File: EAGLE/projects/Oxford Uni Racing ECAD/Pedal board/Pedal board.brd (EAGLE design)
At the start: 165.1 x 216.8 mm, 40 parts, among them IC1 AD711N, J1 ASS + BOTS, J2 THR_1_2, J3 PWR_CAN, J6 BR_POS_PRESS_STWH, J7 T821108A1S100CEU, K2 EC2-12TNU, T1 BT169, X2 D-SUB9-H2M09ST

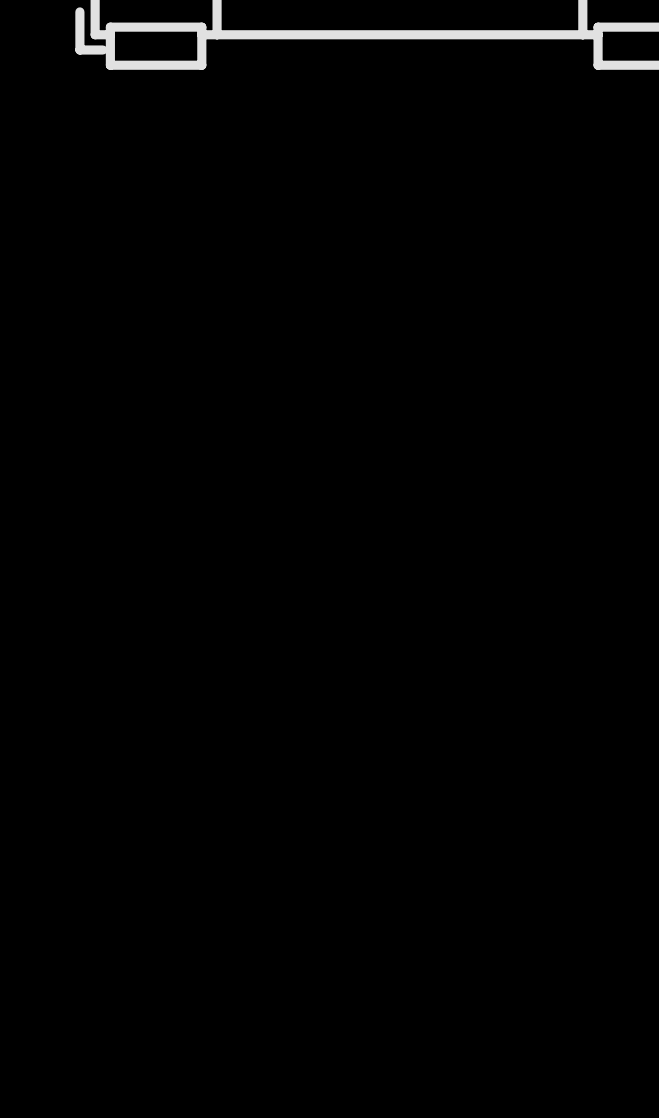
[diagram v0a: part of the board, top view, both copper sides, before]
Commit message: added 1M pullup resistors to analog sensors
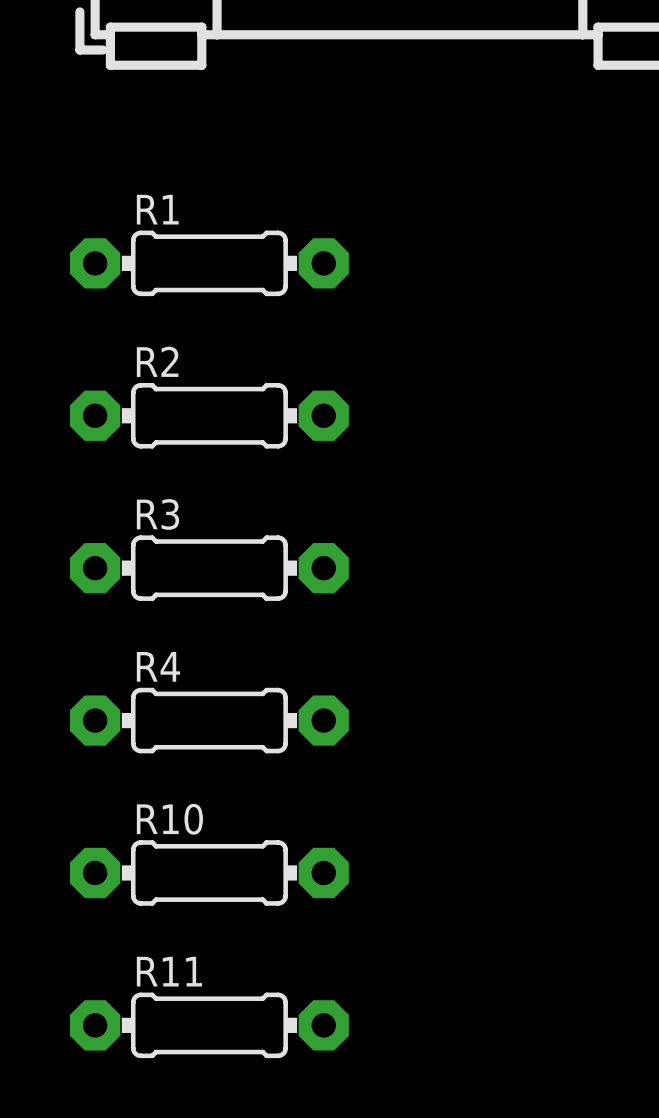
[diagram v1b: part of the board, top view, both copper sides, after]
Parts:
- added R1, R10, R11, R2, R3, R4: 1M, adafruit:0204/7
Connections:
- net 5V: now also R1.2, R10.1, R11.1, R2.1, R3.2, R4.2
- net BR_POSS: now also R10.2
- net BR_POSS2: now also R4.1
- net N$27: now also R11.2
- net ST_WH_POSS: now also R3.1
- net THR1: now also R1.1
- net THR2: now also R2.2
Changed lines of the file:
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@@
 <attribute name="VALUE" x="-74.422" y="-253.492" size="2.54" layer="27"/>
+</element>
+<element name="R1" library="adafruit" library_urn="urn:adsk.eagle:library:420" package="0204/7" package3d_urn="urn:adsk.eagle:package:6240596/1" value="1M" x="-74.93" y="-257.81" smashed="yes">
+<attribute name="NAME" x="-77.47" y="-256.5146" size="0.9906" layer="25" ratio="12"/>
+<attribute name="VALUE" x="-76.5556" y="-258.2926" size="0.9906" layer="27" ratio="12"/>
+</element>
+<element name="R2" library="adafruit" library_urn="urn:adsk.eagle:library:420" package="0204/7" package3d_urn="urn:adsk.eagle:package:6240596/1" value="1M" x="-74.93" y="-262.89" smashed="yes">
+<attribute name="NAME" x="-77.47" y="-261.5946" size="0.9906" layer="25" ratio="12"/>
+<attribute name="VALUE" x="-76.5556" y="-263.3726" size="0.9906" layer="27" ratio="12"/>
+</element>
+<element name="R3" library="adafruit" library_urn="urn:adsk.eagle:library:420" package="0204/7" package3d_urn="urn:adsk.eagle:package:6240596/1" value="1M" x="-74.93" y="-267.97" smashed="yes">
+<attribute name="NAME" x="-77.47" y="-266.6746" size="0.9906" layer="25" ratio="12"/>
+<attribute name="VALUE" x="-76.5556" y="-268.4526" size="0.9906" layer="27" ratio="12"/>
+</element>
+<element name="R4" library="adafruit" library_urn="urn:adsk.eagle:library:420" package="0204/7" package3d_urn="urn:adsk.eagle:package:6240596/1" value="1M" x="-74.93" y="-273.05" smashed="yes">
+<attribute name="NAME" x="-77.47" y="-271.7546" size="0.9906" layer="25" ratio="12"/>
+<attribute name="VALUE" x="-76.5556" y="-273.5326" size="0.9906" layer="27" ratio="12"/>
+</element>
+<element name="R10" library="adafruit" library_urn="urn:adsk.eagle:library:420" package="0204/7" package3d_urn="urn:adsk.eagle:package:6240596/1" value="1M" x="-74.93" y="-278.13" smashed="yes">
+<attribute name="NAME" x="-77.47" y="-276.8346" size="0.9906" layer="25" ratio="12"/>
+<attribute name="VALUE" x="-76.5556" y="-278.6126" size="0.9906" layer="27" ratio="12"/>
+</element>
+<element name="R11" library="adafruit" library_urn="urn:adsk.eagle:library:420" package="0204/7" package3d_urn="urn:adsk.eagle:package:6240596/1" value="1M" x="-74.93" y="-283.21" smashed="yes">
+<attribute name="NAME" x="-77.47" y="-281.9146" size="0.9906" layer="25" ratio="12"/>
+<attribute name="VALUE" x="-76.5556" y="-283.6926" size="0.9906" layer="27" ratio="12"/>
 </element>
 </elements>
@@
 <contactref element="U$1" pad="J802-4"/>
 <contactref element="R21" pad="E"/>
+<contactref element="R10" pad="1"/>
+<contactref element="R4" pad="2"/>
+<contactref element="R11" pad="1"/>
+<contactref element="R3" pad="2"/>
+<contactref element="R2" pad="1"/>
+<contactref element="R1" pad="2"/>
+<wire x1="-71.12" y1="-257.81" x2="-78.74" y2="-171.45" width="0" layer="19" extent="1-1"/>
+<wire x1="-78.74" y1="-262.89" x2="-71.12" y2="-257.81" width="0" layer="19" extent="1-1"/>
+<wire x1="-71.12" y1="-267.97" x2="-78.74" y2="-262.89" width="0" layer="19" extent="1-1"/>
+<wire x1="-71.12" y1="-273.05" x2="-71.12" y2="-267.97" width="0" layer="19" extent="1-1"/>
+<wire x1="-78.74" y1="-278.13" x2="-71.12" y2="-273.05" width="0" layer="19" extent="1-1"/>
+<wire x1="-78.74" y1="-283.21" x2="-78.74" y2="-278.13" width="0" layer="19" extent="1-1"/>
 <wire x1="5.715" y1="-204.47" x2="-78.74" y2="-171.45" width="0" layer="19" extent="1-1"/>
 <wire x1="8.89" y1="-118.11" x2="5.715" y2="-204.47" width="0" layer="19" extent="1-1"/>
@@
 <contactref element="J2" pad="5"/>
 <contactref element="U$1" pad="J803-0"/>
+<contactref element="R1" pad="1"/>
 <wire x1="-78.74" y1="-184.15" x2="152.4" y2="34.29" width="0" layer="19" extent="1-1"/>
+<wire x1="-78.74" y1="-257.81" x2="-78.74" y2="-184.15" width="0" layer="19" extent="1-1"/>
 </signal>
 <signal name="THR2">
 <contactref element="J2" pad="6"/>
 <contactref element="U$1" pad="J803-1"/>
+<contactref element="R2" pad="2"/>
 <wire x1="-78.74" y1="-186.69" x2="152.4" y2="36.83" width="0" layer="19" extent="1-1"/>
+<wire x1="-71.12" y1="-262.89" x2="-78.74" y2="-186.69" width="0" layer="19" extent="1-1"/>
 </signal>
 <signal name="3.3V">
@@
 <contactref element="J6" pad="5"/>
 <contactref element="U$1" pad="J803-3"/>
+<contactref element="R10" pad="2"/>
 <wire x1="-78.74" y1="-191.77" x2="13.97" y2="-120.65" width="0" layer="19" extent="1-1"/>
+<wire x1="-71.12" y1="-278.13" x2="-78.74" y2="-191.77" width="0" layer="19" extent="1-1"/>
 </signal>
 <signal name="BRAKE_LIGHTS_OUT">
@@
 <contactref element="J6" pad="6"/>
 <contactref element="IC1" pad="3"/>
+<contactref element="R11" pad="2"/>
 <wire x1="13.97" y1="-118.11" x2="7.62" y2="-171.45" width="0" layer="19" extent="1-1"/>
+<wire x1="-71.12" y1="-283.21" x2="7.62" y2="-171.45" width="0" layer="19" extent="1-1"/>
 </signal>
 <signal name="BR_PRESS">
@@
 <contactref element="J6" pad="7"/>
 <contactref element="U$1" pad="J803-4"/>
+<contactref element="R4" pad="1"/>
 <wire x1="-78.74" y1="-194.31" x2="16.51" y2="-120.65" width="0" layer="19" extent="1-1"/>
+<wire x1="-78.74" y1="-273.05" x2="-78.74" y2="-194.31" width="0" layer="19" extent="1-1"/>
 </signal>
 <signal name="ST_WH_POSS">
 <contactref element="J6" pad="8"/>
 <contactref element="U$1" pad="J803-5"/>
+<contactref element="R3" pad="1"/>
 <wire x1="-78.74" y1="-196.85" x2="16.51" y2="-118.11" width="0" layer="19" extent="1-1"/>
+<wire x1="-78.74" y1="-267.97" x2="-78.74" y2="-196.85" width="0" layer="19" extent="1-1"/>
 </signal>
 <signal name="12V_BATTERY">

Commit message: fixed overlapping digital pins
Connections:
- net BR_POSS: now also U$1.J803-2; no longer U$1.J803-3
- net BR_POSS2: now also U$1.J803-3; no longer U$1.J803-4
- net BR_PRESS: now also U$1.J803-4; no longer U$1.J803-2
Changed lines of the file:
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@@
 <signal name="BR_POSS">
 <contactref element="J6" pad="5"/>
-<contactref element="U$1" pad="J803-3"/>
 <contactref element="R10" pad="2"/>
-<wire x1="-78.74" y1="-191.77" x2="13.97" y2="-120.65" width="0" layer="19" extent="1-1"/>
-<wire x1="-71.12" y1="-278.13" x2="-78.74" y2="-191.77" width="0" layer="19" extent="1-1"/>
+<contactref element="U$1" pad="J803-2"/>
+<wire x1="-78.74" y1="-189.23" x2="13.97" y2="-120.65" width="0" layer="19" extent="1-1"/>
+<wire x1="-71.12" y1="-278.13" x2="-78.74" y2="-189.23" width="0" layer="19" extent="1-1"/>
 </signal>
 <signal name="BRAKE_LIGHTS_OUT">
@@
 <contactref element="COMPARATOR" pad="5"/>
 <wire x1="8.190228125" y1="-68.94195" x2="11.504928125" y2="-68.94195" width="0.8128" layer="16"/>
-<contactref element="U$1" pad="J803-2"/>
+<contactref element="U$1" pad="J803-4"/>
 <wire x1="7.62" y1="-181.61" x2="0" y2="-176.53" width="0" layer="19" extent="1-1"/>
-<wire x1="-78.74" y1="-189.23" x2="0" y2="-176.53" width="0" layer="19" extent="1-1"/>
+<wire x1="-78.74" y1="-194.31" x2="0" y2="-176.53" width="0" layer="19" extent="1-1"/>
 <wire x1="8.190228125" y1="-68.94195" x2="0" y2="-176.53" width="0" layer="19" extent="16-16"/>
 </signal>
@@
 <signal name="BR_POSS2">
 <contactref element="J6" pad="7"/>
-<contactref element="U$1" pad="J803-4"/>
 <contactref element="R4" pad="1"/>
-<wire x1="-78.74" y1="-194.31" x2="16.51" y2="-120.65" width="0" layer="19" extent="1-1"/>
-<wire x1="-78.74" y1="-273.05" x2="-78.74" y2="-194.31" width="0" layer="19" extent="1-1"/>
+<contactref element="U$1" pad="J803-3"/>
+<wire x1="-78.74" y1="-191.77" x2="16.51" y2="-120.65" width="0" layer="19" extent="1-1"/>
+<wire x1="-78.74" y1="-273.05" x2="-78.74" y2="-191.77" width="0" layer="19" extent="1-1"/>
 </signal>
 <signal name="ST_WH_POSS">

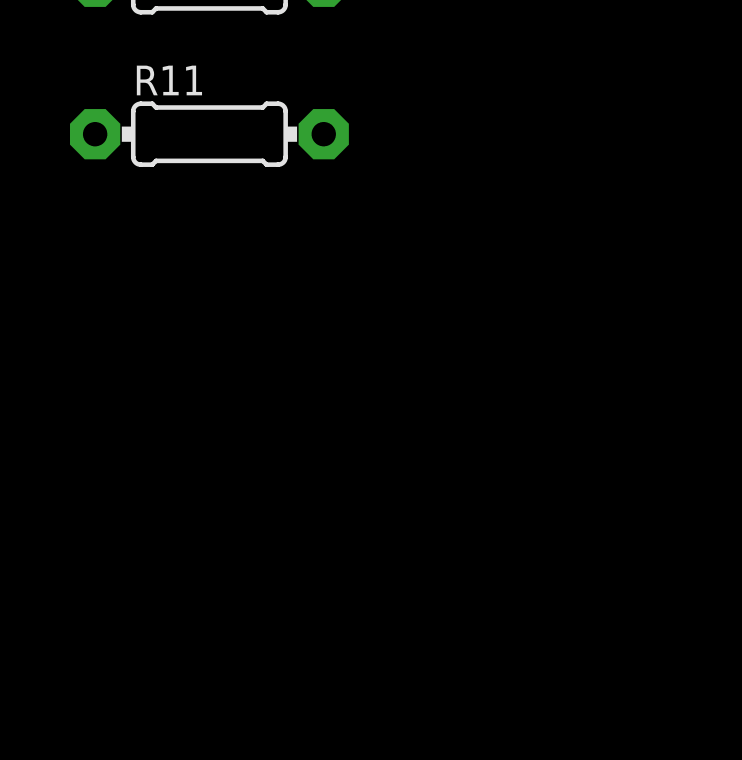
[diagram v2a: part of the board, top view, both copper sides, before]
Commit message: added indicator LEDs to boards
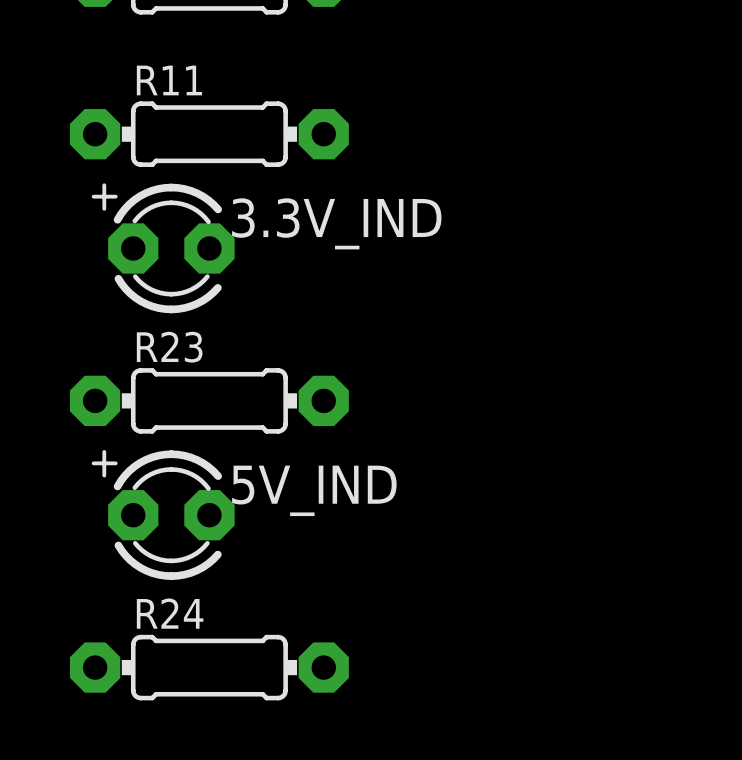
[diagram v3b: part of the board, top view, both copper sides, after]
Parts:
- added 3.3V_IND, 5V_IND: (no value), adafruit:LED3MM
- added R23, R24: (no value), adafruit:0204/7
- BRAKE_LIGHTS: value 2A -> 1A
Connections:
- new net N$12: 3.3V_IND.K, R23.2
- new net N$4: 5V_IND.K, R24.2
- net 3.3V: now also 3.3V_IND.A
- net 5V: now also 5V_IND.A
- net GND: now also R23.1, R24.1
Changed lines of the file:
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@@
 <attribute name="VALUE" x="-74.422" y="-238.252" size="2.54" layer="27"/>
 </element>
-<element name="BRAKE_LIGHTS" library="fuse" library_urn="urn:adsk.eagle:library:233" package="FUSE_HOLDER_5X20MM" package3d_urn="urn:adsk.eagle:package:14079/1" value="2A" x="-76.2" y="-247.65" smashed="yes">
+<element name="BRAKE_LIGHTS" library="fuse" library_urn="urn:adsk.eagle:library:233" package="FUSE_HOLDER_5X20MM" package3d_urn="urn:adsk.eagle:package:14079/1" value="1A" x="-76.2" y="-247.65" smashed="yes">
 <attribute name="MF" value="" x="-76.2" y="-247.65" size="1.778" layer="27" display="off"/>
 <attribute name="MPN" value="" x="-76.2" y="-247.65" size="1.778" layer="27" display="off"/>
@@
 <attribute name="NAME" x="-77.47" y="-281.9146" size="0.9906" layer="25" ratio="12"/>
 <attribute name="VALUE" x="-76.5556" y="-283.6926" size="0.9906" layer="27" ratio="12"/>
+</element>
+<element name="3.3V_IND" library="adafruit" library_urn="urn:adsk.eagle:library:420" package="LED3MM" package3d_urn="urn:adsk.eagle:package:6240537/1" value="" x="-76.2" y="-287.02" smashed="yes">
+<attribute name="NAME" x="-74.295" y="-286.639" size="1.27" layer="25" ratio="10"/>
+<attribute name="VALUE" x="-74.295" y="-288.671" size="1.27" layer="27" ratio="10"/>
+</element>
+<element name="R23" library="adafruit" library_urn="urn:adsk.eagle:library:420" package="0204/7" package3d_urn="urn:adsk.eagle:package:6240596/1" value="" x="-74.93" y="-292.1" smashed="yes">
+<attribute name="NAME" x="-77.47" y="-290.8046" size="0.9906" layer="25" ratio="12"/>
+<attribute name="VALUE" x="-76.5556" y="-292.5826" size="0.9906" layer="27" ratio="12"/>
+</element>
+<element name="5V_IND" library="adafruit" library_urn="urn:adsk.eagle:library:420" package="LED3MM" package3d_urn="urn:adsk.eagle:package:6240537/1" value="" x="-76.2" y="-295.91" smashed="yes">
+<attribute name="NAME" x="-74.295" y="-295.529" size="1.27" layer="25" ratio="10"/>
+<attribute name="VALUE" x="-74.295" y="-297.561" size="1.27" layer="27" ratio="10"/>
+</element>
+<element name="R24" library="adafruit" library_urn="urn:adsk.eagle:library:420" package="0204/7" package3d_urn="urn:adsk.eagle:package:6240596/1" value="" x="-74.93" y="-300.99" smashed="yes">
+<attribute name="NAME" x="-77.47" y="-299.6946" size="0.9906" layer="25" ratio="12"/>
+<attribute name="VALUE" x="-76.5556" y="-301.4726" size="0.9906" layer="27" ratio="12"/>
 </element>
 </elements>
@@
 <contactref element="U$1" pad="J802-5"/>
 <contactref element="U$1" pad="J802-6"/>
+<contactref element="R24" pad="1"/>
+<contactref element="R23" pad="1"/>
 <wire x1="-78.74" y1="-176.53" x2="-78.74" y2="-173.99" width="0" layer="19" extent="1-1"/>
 <wire x1="0" y1="-181.61" x2="-78.74" y2="-176.53" width="0" layer="19" extent="1-1"/>
@@
 <wire x1="149.86" y1="34.29" x2="134.62" y2="22.86" width="0" layer="19" extent="16-16"/>
 <wire x1="149.86" y1="36.83" x2="149.86" y2="34.29" width="0" layer="19" extent="1-1"/>
+<wire x1="-78.74" y1="-292.1" x2="-78.74" y2="-176.53" width="0" layer="19" extent="1-1"/>
+<wire x1="-78.74" y1="-300.99" x2="-78.74" y2="-292.1" width="0" layer="19" extent="1-1"/>
 </signal>
 <signal name="N$7">
@@
 <contactref element="R2" pad="1"/>
 <contactref element="R1" pad="2"/>
+<contactref element="5V_IND" pad="A"/>
 <wire x1="-71.12" y1="-257.81" x2="-78.74" y2="-171.45" width="0" layer="19" extent="1-1"/>
 <wire x1="-78.74" y1="-262.89" x2="-71.12" y2="-257.81" width="0" layer="19" extent="1-1"/>
@@
 <wire x1="-78.74" y1="-278.13" x2="-71.12" y2="-273.05" width="0" layer="19" extent="1-1"/>
 <wire x1="-78.74" y1="-283.21" x2="-78.74" y2="-278.13" width="0" layer="19" extent="1-1"/>
+<wire x1="-77.47" y1="-295.91" x2="-78.74" y2="-283.21" width="0" layer="19" extent="1-1"/>
 <wire x1="5.715" y1="-204.47" x2="-78.74" y2="-171.45" width="0" layer="19" extent="1-1"/>
 <wire x1="8.89" y1="-118.11" x2="5.715" y2="-204.47" width="0" layer="19" extent="1-1"/>
@@
 <wire x1="116.84" y1="21.59" x2="114.3" y2="21.59" width="1.27" layer="16"/>
 <contactref element="J6" pad="1"/>
+<contactref element="3.3V_IND" pad="A"/>
 <wire x1="8.89" y1="-120.65" x2="114.3" y2="7.62" width="0" layer="19" extent="1-1"/>
+<wire x1="-77.47" y1="-287.02" x2="8.89" y2="-120.65" width="0" layer="19" extent="1-1"/>
 </signal>
 <signal name="BR_POSS">
@@
 <wire x1="-60.96" y1="-247.65" x2="16.51" y2="-138.43" width="0" layer="19" extent="1-1"/>
 </signal>
+<signal name="N$4">
+<contactref element="5V_IND" pad="K"/>
+<contactref element="R24" pad="2"/>
+<wire x1="-74.93" y1="-295.91" x2="-71.12" y2="-300.99" width="0" layer="19" extent="1-1"/>
+</signal>
+<signal name="N$12">
+<contactref element="R23" pad="2"/>
+<contactref element="3.3V_IND" pad="K"/>
+<wire x1="-74.93" y1="-287.02" x2="-71.12" y2="-292.1" width="0" layer="19" extent="1-1"/>
+</signal>
 </signals>
